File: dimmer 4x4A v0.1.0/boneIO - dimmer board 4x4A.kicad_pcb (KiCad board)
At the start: 2 copper layers, 67.8 x 86.9 mm, 107 parts, among them J1 Screw_Terminal_01x02, J2 Jumper 60.4R, J3 Jumper 60.4R, J4 Jumper 120R, J5 RGBW, J6 PROG, J7 CAN&RS, J8 Screw_Terminal_01x08, Q1 BC817, Q10 BSS138, Q11 BSS138, Q12 BSS138, Q2 BC817, Q3 PSMN1R2-30YLC, Q4 PSMN1R2-30YLC, Q5 BC817, Q6 BC817, Q7 BC807, Q8 PSMN1R2-30YLC, Q9 PSMN1R2-30YLC, U1 SN65HVD230, U2 5V, U3 AMS1117-3.3, U4 MAX485E, U5 WT32-ETH01

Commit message: add GND
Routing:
- net GND: vias 12 -> 1093

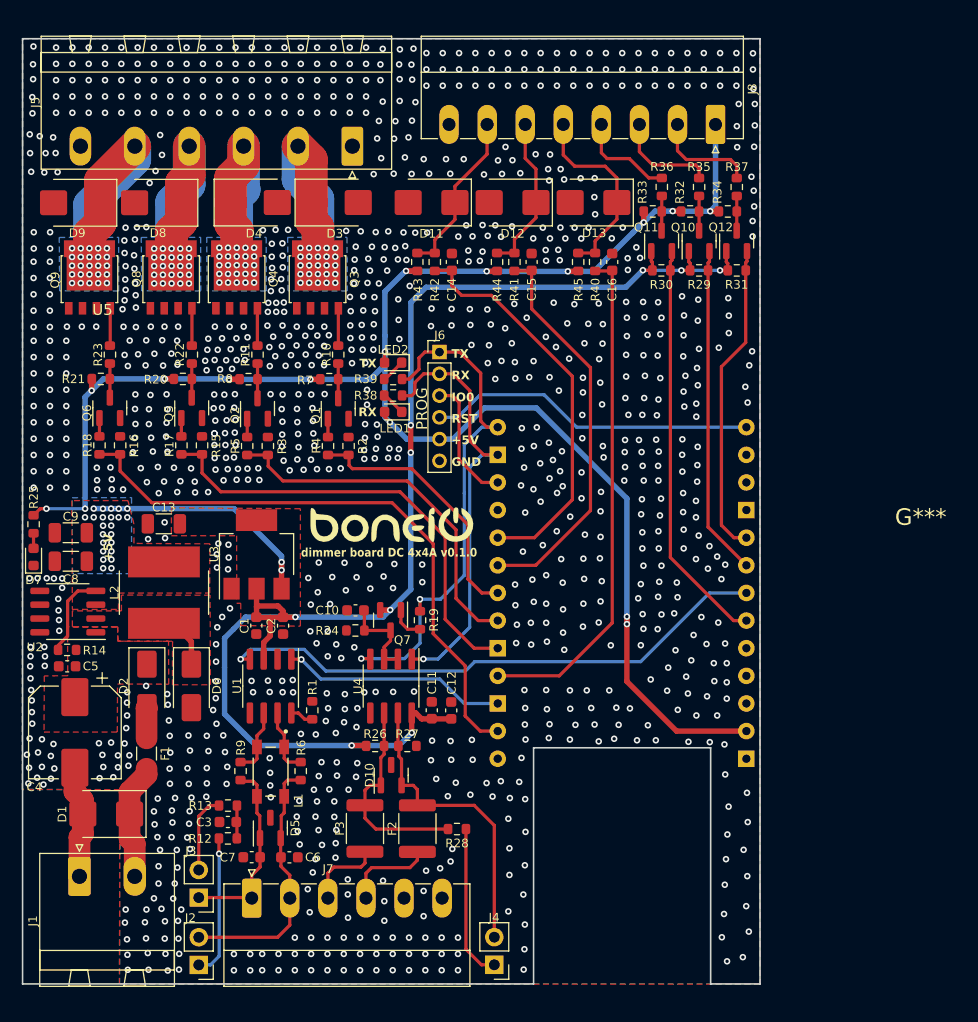
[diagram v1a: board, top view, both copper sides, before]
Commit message: przesuniecie zlaczy
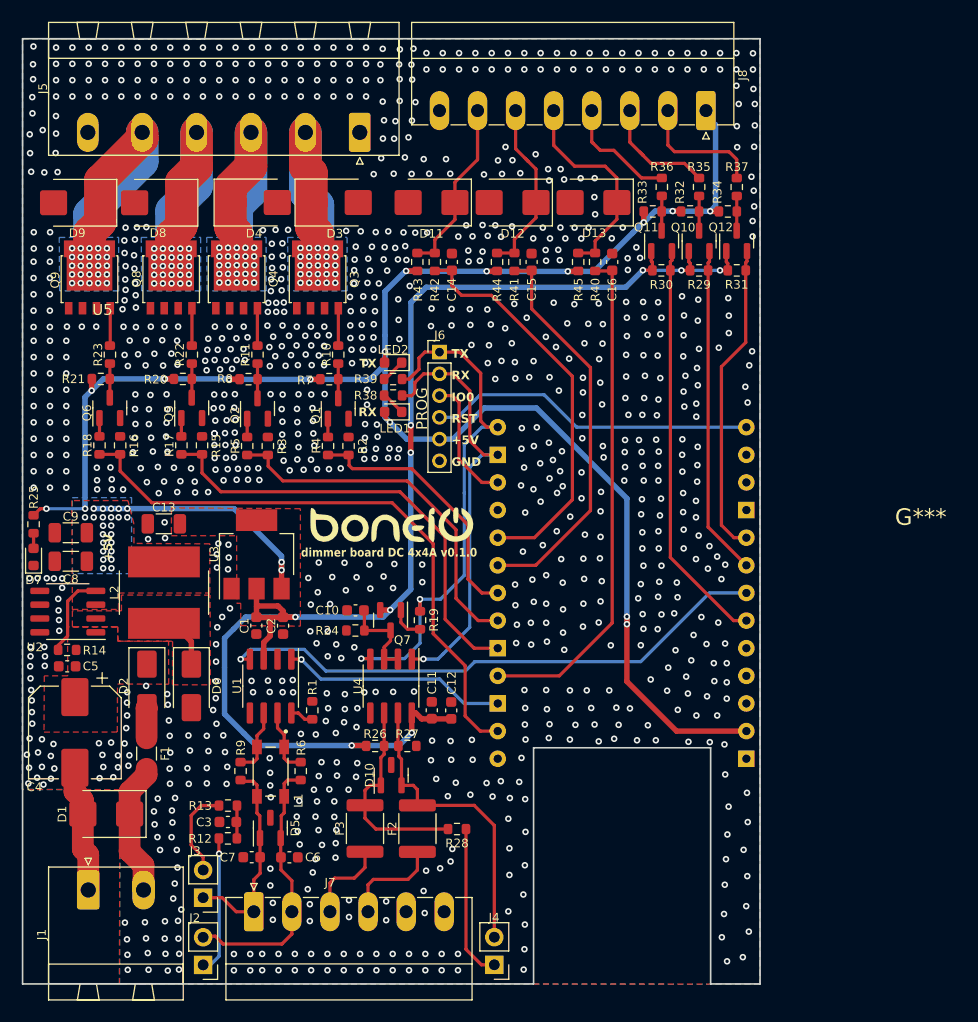
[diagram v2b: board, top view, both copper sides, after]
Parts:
- moved J8 1.55 mm to (157.9, 49.2)
- moved J1 1.49 mm to (101.2, 120.8)
- moved J5 1.44 mm to (126.1, 51.2)
- moved J7 1.27 mm to (116.4, 122.8)
- moved J3 0.40 mm to (111.7, 121.5)
- moved J2 0.40 mm to (111.7, 127.7)
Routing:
- net CAN_H: track 24.0 -> 27.4 mm
- net BLUE_OUT: track 24.1 -> 27.3 mm
- net WHITE_OUT: track 26.2 -> 29.3 mm
- net WS281x1_OUT: track 9.57 -> 11.8 mm
- net Net-(J3-Pin_2): track 7.21 -> 9.29 mm
- net Net-(D12-K): track 14.7 -> 16.7 mm
- net Net-(D13-K): track 17.9 -> 19.5 mm
- net VDD: track 10.7 -> 12.3 mm
- net WS281x2_OUT: track 9.51 -> 11.1 mm
- net WS281x3_OUT: track 9.13 -> 10.7 mm
- net CAN_L: track 17.4 -> 19.0 mm
- net GREEN_OUT: track 24.5 -> 26.0 mm
- net GND: track 10.6 -> 12.0 mm, vias 1093 -> 1028
- net RED_OUT: track 25.0 -> 26.2 mm
- net B-_OUT: track 8.27 -> 9.25 mm
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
